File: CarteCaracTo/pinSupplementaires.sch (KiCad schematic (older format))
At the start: 2 parts

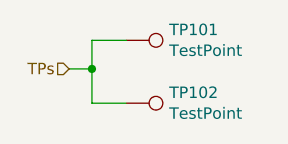
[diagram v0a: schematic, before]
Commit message: Mise en forme de la carte + version carte ASIC et Carac separées
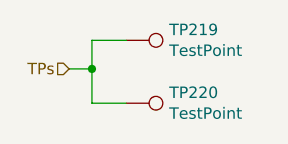
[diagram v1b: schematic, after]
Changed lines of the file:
@@
 $Descr A4 11693 8268
 encoding utf-8
-Sheet 96 123
+Sheet 36 123
 Title ""
 Date ""
@@
 AR Path="/61C00939/61AEFC16/61AEBA54/60EE2C0D" Ref="TP137"  Part="1"
 AR Path="/61C00939/61AEFC16/61AEBA57/60EE2C0D" Ref="TP139"  Part="1"
-F 0 "TP101" V 3004 2013 50  0000 L CNN
+F 0 "TP219" V 3004 2013 50  0000 L CNN
 F 1 "TestPoint" V 3095 2013 50  0000 L CNN
 F 2 "Connector_PinHeader_2.54mm:PinHeader_1x01_P2.54mm_Vertical" H 3250 1825 50  0001 C CNN
@@
 AR Path="/61C00939/61AEFC16/61AEBA54/60EE3798" Ref="TP138"  Part="1"
 AR Path="/61C00939/61AEFC16/61AEBA57/60EE3798" Ref="TP140"  Part="1"
-F 0 "TP102" V 3004 2288 50  0000 L CNN
+F 0 "TP220" V 3004 2288 50  0000 L CNN
 F 1 "TestPoint" V 3095 2288 50  0000 L CNN
 F 2 "Connector_PinHeader_2.54mm:PinHeader_1x01_P2.54mm_Vertical" H 3250 2100 50  0001 C CNN

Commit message: ID des pins, option capa sur sortie, option GND ou plan de masse sur BNC
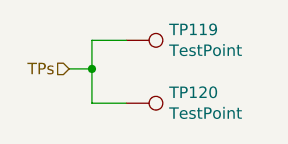
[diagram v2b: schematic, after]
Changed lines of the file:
@@
 AR Path="/61C00939/61AEFC16/61AEBA54/60EE2C0D" Ref="TP137"  Part="1"
 AR Path="/61C00939/61AEFC16/61AEBA57/60EE2C0D" Ref="TP139"  Part="1"
-F 0 "TP219" V 3004 2013 50  0000 L CNN
+F 0 "TP119" V 3004 2013 50  0000 L CNN
 F 1 "TestPoint" V 3095 2013 50  0000 L CNN
 F 2 "Connector_PinHeader_2.54mm:PinHeader_1x01_P2.54mm_Vertical" H 3250 1825 50  0001 C CNN
@@
 AR Path="/61C00939/61AEFC16/61AEBA54/60EE3798" Ref="TP138"  Part="1"
 AR Path="/61C00939/61AEFC16/61AEBA57/60EE3798" Ref="TP140"  Part="1"
-F 0 "TP220" V 3004 2288 50  0000 L CNN
+F 0 "TP120" V 3004 2288 50  0000 L CNN
 F 1 "TestPoint" V 3095 2288 50  0000 L CNN
 F 2 "Connector_PinHeader_2.54mm:PinHeader_1x01_P2.54mm_Vertical" H 3250 2100 50  0001 C CNN

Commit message: Routé, verif pre-envoie
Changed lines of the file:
@@
 $Descr A4 11693 8268
 encoding utf-8
-Sheet 36 122
+Sheet 80 122
 Title ""
 Date ""
@@
 AR Path="/61C00939/61AEFC16/61AEBA54/60EE2C0D" Ref="TP137"  Part="1"
 AR Path="/61C00939/61AEFC16/61AEBA57/60EE2C0D" Ref="TP139"  Part="1"
-F 0 "TP119" V 3004 2013 50  0000 L CNN
+F 0 "TP295" V 3004 2013 50  0000 L CNN
 F 1 "TestPoint" V 3095 2013 50  0000 L CNN
 F 2 "Connector_PinHeader_2.54mm:PinHeader_1x01_P2.54mm_Vertical" H 3250 1825 50  0001 C CNN
@@
 AR Path="/61C00939/61AEFC16/61AEBA54/60EE3798" Ref="TP138"  Part="1"
 AR Path="/61C00939/61AEFC16/61AEBA57/60EE3798" Ref="TP140"  Part="1"
-F 0 "TP120" V 3004 2288 50  0000 L CNN
+F 0 "TP296" V 3004 2288 50  0000 L CNN
 F 1 "TestPoint" V 3095 2288 50  0000 L CNN
 F 2 "Connector_PinHeader_2.54mm:PinHeader_1x01_P2.54mm_Vertical" H 3250 2100 50  0001 C CNN

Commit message: Envoyé en prod
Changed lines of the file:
@@
 $Descr A4 11693 8268
 encoding utf-8
-Sheet 80 122
+Sheet 81 122
 Title ""
 Date ""
@@
 AR Path="/61C00939/61AEFC16/61AEBA54/60EE2C0D" Ref="TP137"  Part="1"
 AR Path="/61C00939/61AEFC16/61AEBA57/60EE2C0D" Ref="TP139"  Part="1"
-F 0 "TP295" V 3004 2013 50  0000 L CNN
+F 0 "TP297" V 3004 2013 50  0000 L CNN
 F 1 "TestPoint" V 3095 2013 50  0000 L CNN
 F 2 "Connector_PinHeader_2.54mm:PinHeader_1x01_P2.54mm_Vertical" H 3250 1825 50  0001 C CNN
@@
 AR Path="/61C00939/61AEFC16/61AEBA54/60EE3798" Ref="TP138"  Part="1"
 AR Path="/61C00939/61AEFC16/61AEBA57/60EE3798" Ref="TP140"  Part="1"
-F 0 "TP296" V 3004 2288 50  0000 L CNN
+F 0 "TP298" V 3004 2288 50  0000 L CNN
 F 1 "TestPoint" V 3095 2288 50  0000 L CNN
 F 2 "Connector_PinHeader_2.54mm:PinHeader_1x01_P2.54mm_Vertical" H 3250 2100 50  0001 C CNN
